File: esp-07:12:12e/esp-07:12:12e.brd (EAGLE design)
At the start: 40.3 x 38.1 mm, 5 parts, among them J1 ESP-STACK-HEADER

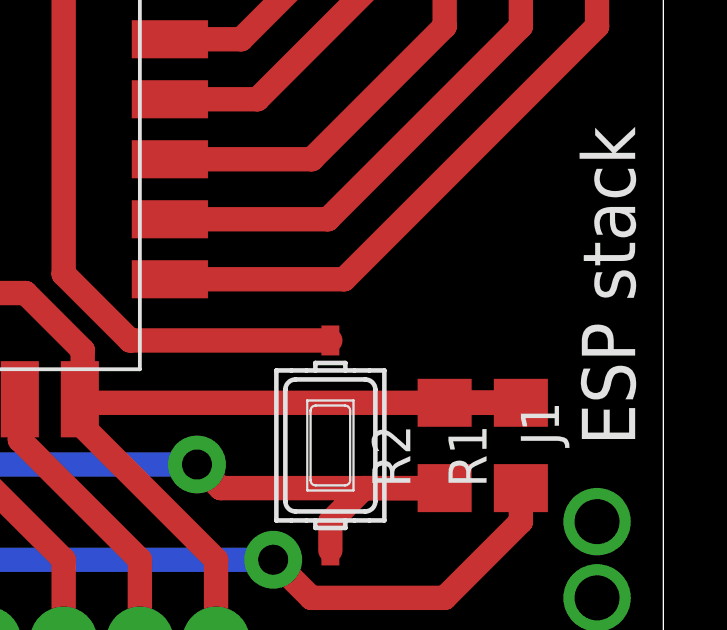
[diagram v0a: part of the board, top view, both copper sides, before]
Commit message: Added capacitor for power stability
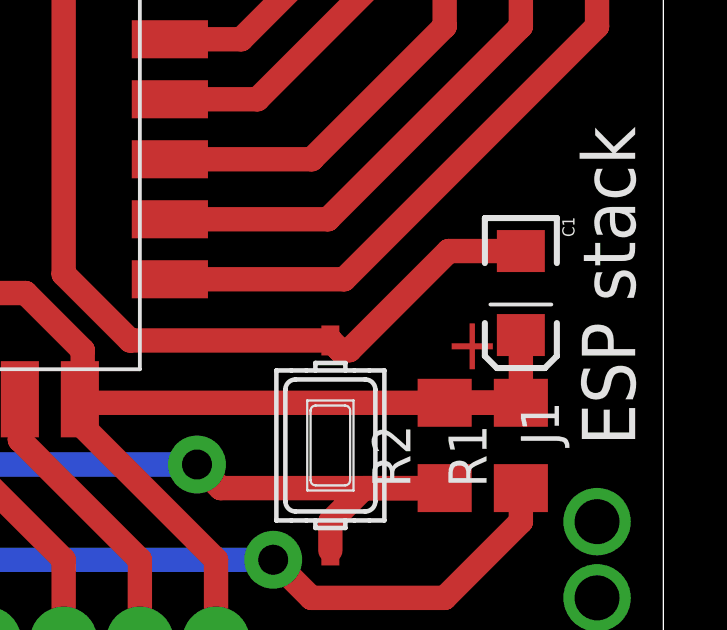
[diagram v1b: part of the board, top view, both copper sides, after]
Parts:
- added C1: 10uF, SparkFun-Capacitors:EIA3216
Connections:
- net +3V3: now also C1.A
- net GND: now also C1.C
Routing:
- net GND: track 56.0 -> 63.9 mm
- net +3V3: track 59.7 -> 61.9 mm
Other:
- board text added: "+"

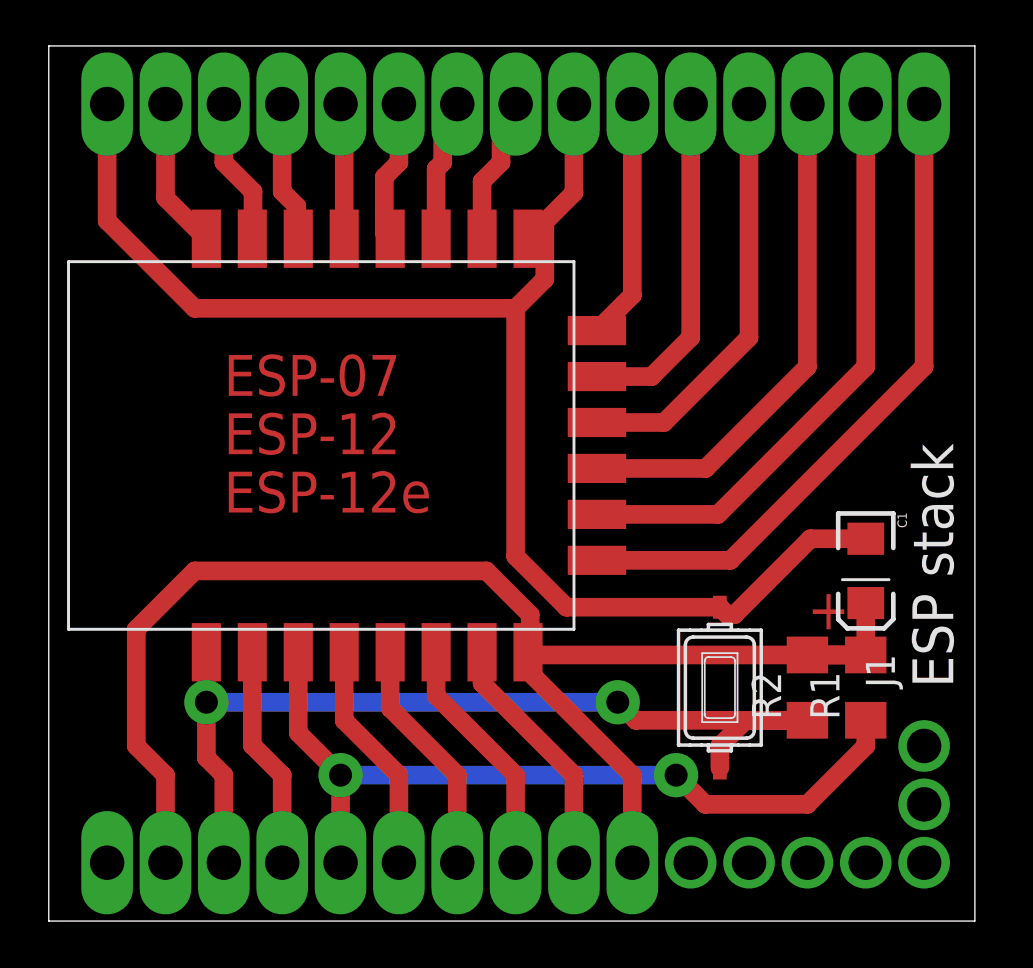
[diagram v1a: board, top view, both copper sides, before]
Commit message: Fix paths under ESP board - shouldn't overlap with module pads
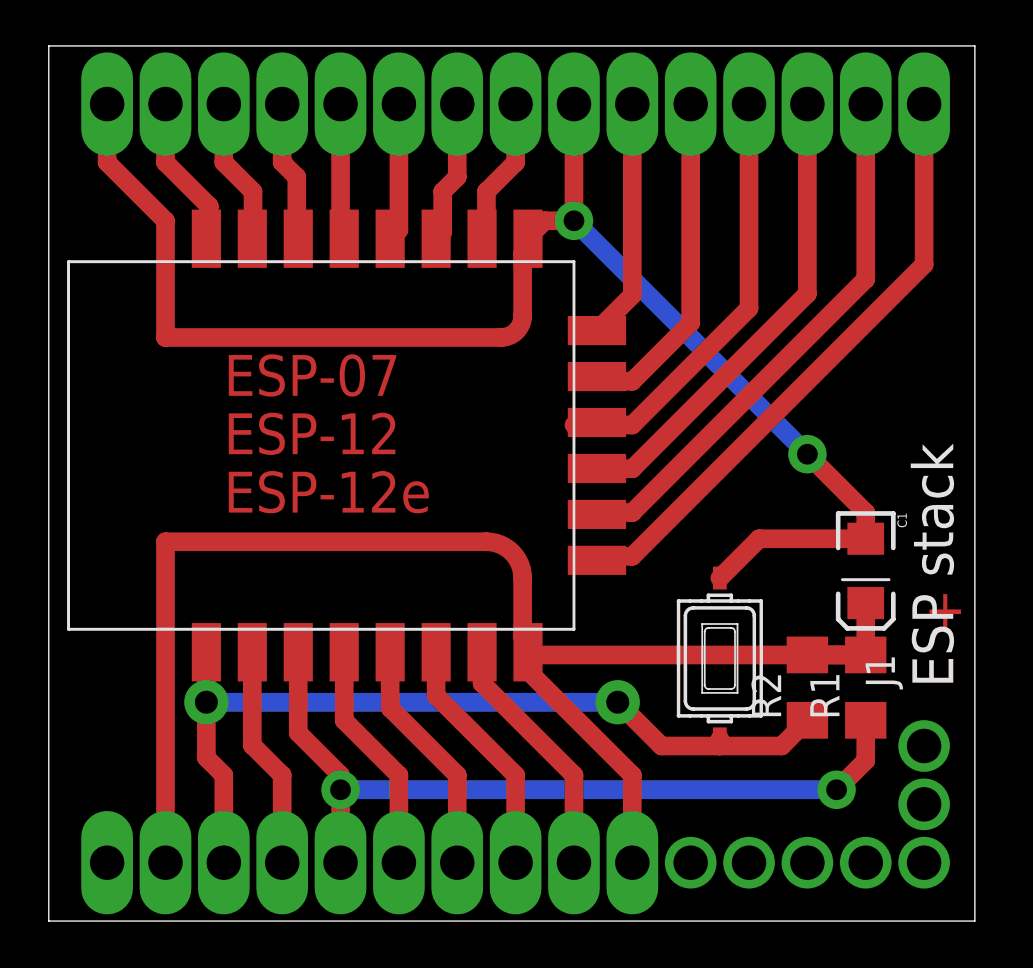
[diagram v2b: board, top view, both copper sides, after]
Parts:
- moved RESET 1.27 mm to (29.2, 11.4)
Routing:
- net RESET: track 41.2 -> 37.2 mm
- net CS0: track 29.2 -> 26.6 mm
- net MISO: track 25.8 -> 23.6 mm
- net +3V3: track 61.9 -> 64.1 mm
- net GPIO9: track 22.4 -> 20.6 mm
- net GND: track 63.9 -> 64.2 mm, vias 0 -> 2

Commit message: New board size - 1.4 inches; reduced number of signal pins to only two; mounting holes
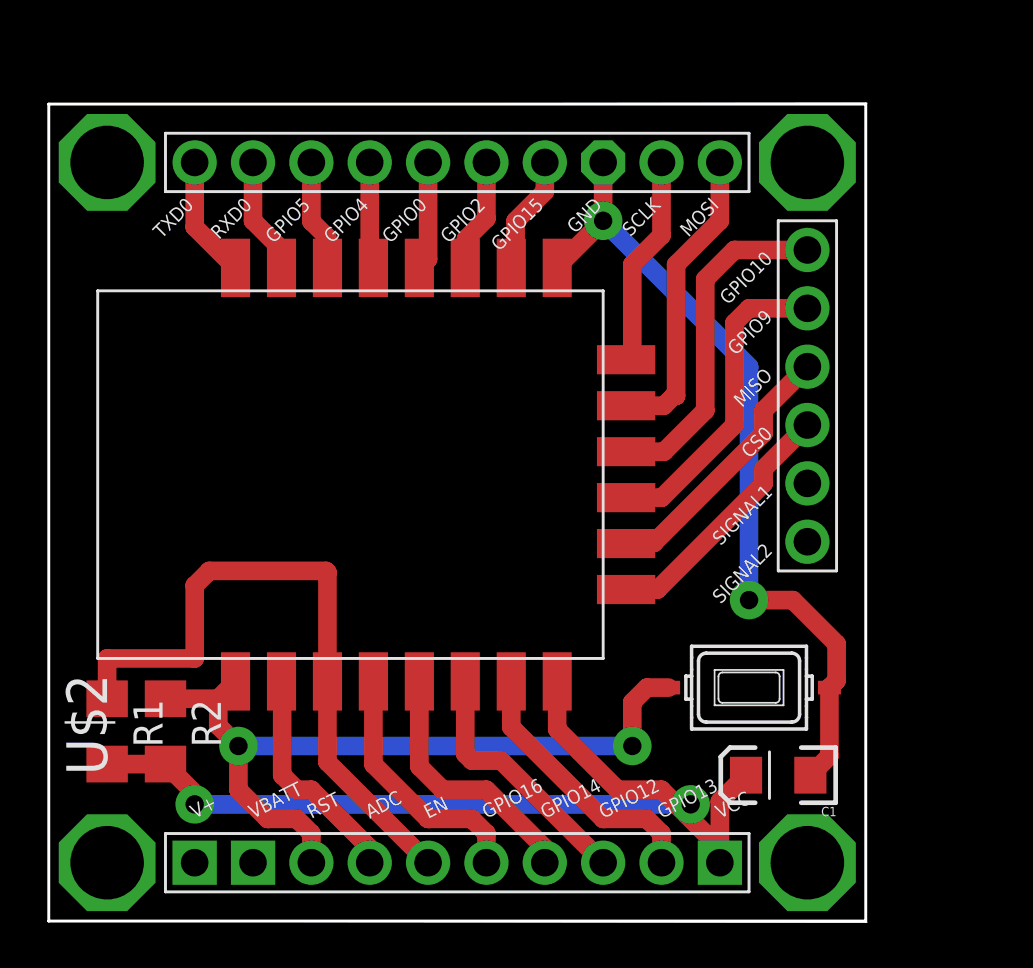
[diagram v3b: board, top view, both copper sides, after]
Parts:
- removed J1: ESP-STACK-HEADER, ESPstack:ESP-STACK-HEADER
- added U$2: ESP-BOARD, ESPstack:ESP-BOARD
- moved R1 33.1 mm to (2.54, 8.26), turned to 270 degrees
- moved R2 28.0 mm to (5.08, 8.26), turned to 270 degrees
- moved C1 9.67 mm to (31.8, 6.35), turned to 180 degrees
- moved RESET 1.80 mm to (30.5, 10.2), turned to 180 degrees
- moved U$1 1.80 mm to (24.1, 11.4)
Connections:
- new net VBATT: U$2.VBATT
- net +3V3: now also U$2.VCC; no longer J1.3V3@1, J1.3V3@2
- net ADC: now also U$2.ADC; no longer J1.ADC
- net CS0: now also U$2.CS0; no longer J1.CS0
- net EN: now also U$2.EN; no longer J1.EN
- net GND: now also U$2.GND@1, U$2.GND@2, U$2.GND@3, U$2.GND@4, U$2.GND@5; no longer J1.GND@1, J1.GND@2
- net GPIO0: now also U$2.GPIO0; no longer J1.GPIO0
- net GPIO10: now also U$2.GPIO10; no longer J1.GPIO10
- net GPIO12: now also U$2.GPIO12; no longer J1.GPIO12
- net GPIO13: now also U$2.GPIO13; no longer J1.GPIO13
- net GPIO14: now also U$2.GPIO14; no longer J1.GPIO14
- net GPIO15: now also U$2.GPIO15; no longer J1.GPIO15
- net GPIO16: now also U$2.GPIO16; no longer J1.GPIO16
- net GPIO2: now also U$2.GPIO2; no longer J1.GPIO2
- net GPIO4: now also U$2.GPIO4; no longer J1.GPIO4
- net GPIO5: now also U$2.GPIO5; no longer J1.GPIO5
- net GPIO9: now also U$2.GPIO9; no longer J1.GPIO9
- net MISO: now also U$2.MISO; no longer J1.MISO
- net MOSI: now also U$2.MOSI; no longer J1.MOSI
- net RESET: now also U$2.RST; no longer J1.RESET
- net RXD0: now also U$2.RXD0; no longer J1.RXD0
- net SCLK: now also U$2.SCLK; no longer J1.SCLK
- net TXD0: now also U$2.TXD0; no longer J1.TXD0
- net V+: now also U$2.V+; no longer J1.VBAT
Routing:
- net GND: track 64.2 -> 35.3 mm
- net +3V3: track 64.1 -> 43.1 mm, vias 0 -> 2
- net CS0: track 26.6 -> 11.2 mm
- net MISO: track 23.6 -> 11.7 mm
- net GPIO9: track 20.6 -> 13.9 mm
- net EN: track 35.1 -> 29.3 mm, vias 2 -> 0
- net GPIO10: track 18.8 -> 14.9 mm
- net RESET: track 37.2 -> 33.8 mm
- net MOSI: track 14.7 -> 13.3 mm
- net TXD0: track 6.70 -> 5.33 mm
- net GPIO2: track 6.24 -> 4.97 mm
- net GPIO4: track 5.93 -> 4.66 mm
- net GPIO15: track 6.46 -> 5.19 mm
- net GPIO0: track 6.02 -> 4.75 mm
- net GPIO5: track 6.15 -> 4.88 mm
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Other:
- board size 40.3 x 38.1 mm -> 35.6 x 35.7 mm
- board text removed: "+"
- board text removed: "ESP-07"
- board text removed: "ESP-12"
- board text removed: "ESP-12e"

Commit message: Small clearance improvements, bigger header pads and mounting holes
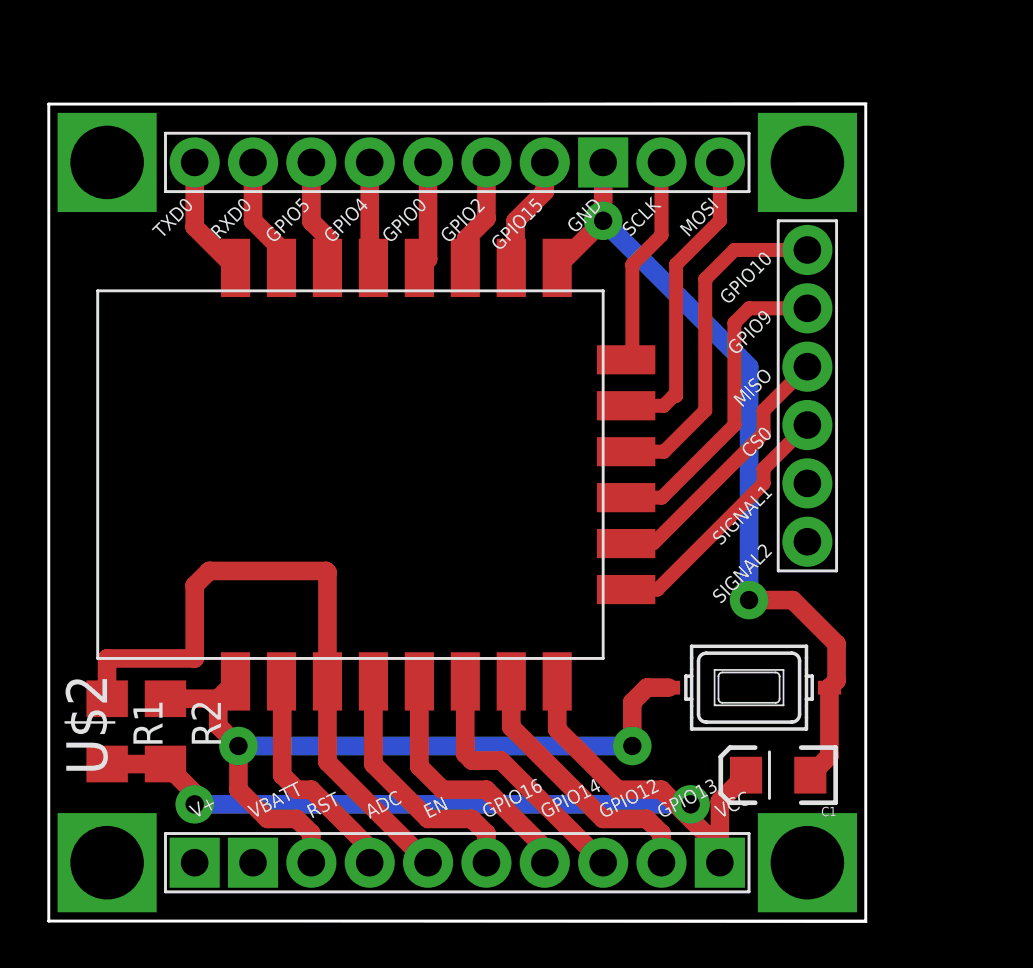
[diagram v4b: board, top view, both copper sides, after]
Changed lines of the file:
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@@
 <contactref element="U$1" pad="SCLK"/>
 <contactref element="U$2" pad="SCLK"/>
-<wire x1="26.67" y1="33.02" x2="26.67" y2="29.845" width="0.8128" layer="1"/>
-<wire x1="26.67" y1="29.845" x2="25.4" y2="28.575" width="0.8128" layer="1"/>
-<wire x1="25.4" y1="28.575" x2="25.4" y2="24.7" width="0.8128" layer="1"/>
+<wire x1="26.67" y1="33.02" x2="26.67" y2="29.845" width="0.6096" layer="1"/>
+<wire x1="26.67" y1="29.845" x2="25.4" y2="28.575" width="0.6096" layer="1"/>
+<wire x1="25.4" y1="28.575" x2="25.4" y2="24.7" width="0.6096" layer="1"/>
 <wire x1="25.4" y1="24.7" x2="25.13" y2="24.43" width="0.8128" layer="1"/>
 </signal>
@@
 <contactref element="U$1" pad="MOSI"/>
 <contactref element="U$2" pad="MOSI"/>
-<wire x1="29.21" y1="33.02" x2="29.21" y2="30.48" width="0.8128" layer="1"/>
-<wire x1="29.21" y1="30.48" x2="27.305" y2="28.575" width="0.8128" layer="1"/>
-<wire x1="27.305" y1="28.575" x2="27.305" y2="22.86" width="0.8128" layer="1"/>
-<wire x1="27.305" y1="22.86" x2="27.2034" y2="22.86" width="0.8128" layer="1"/>
-<wire x1="27.2034" y1="22.86" x2="26.7716" y2="22.4282" width="0.8128" layer="1"/>
-<wire x1="26.7716" y1="22.4282" x2="25.1318" y2="22.4282" width="0.8128" layer="1"/>
+<wire x1="29.21" y1="33.02" x2="29.21" y2="30.48" width="0.6096" layer="1"/>
+<wire x1="29.21" y1="30.48" x2="27.305" y2="28.575" width="0.6096" layer="1"/>
+<wire x1="27.305" y1="28.575" x2="27.305" y2="22.86" width="0.6096" layer="1"/>
+<wire x1="27.305" y1="22.86" x2="27.2034" y2="22.86" width="0.6096" layer="1"/>
+<wire x1="27.2034" y1="22.86" x2="26.7716" y2="22.4282" width="0.6096" layer="1"/>
+<wire x1="26.7716" y1="22.4282" x2="25.1318" y2="22.4282" width="0.6096" layer="1"/>
 <wire x1="25.1318" y1="22.4282" x2="25.13" y2="22.43" width="0.8128" layer="1"/>
 </signal>
@@
 <contactref element="U$1" pad="GPIO10"/>
 <contactref element="U$2" pad="GPIO10"/>
-<wire x1="25.13" y1="20.43" x2="26.78" y2="20.43" width="0.8128" layer="1"/>
-<wire x1="26.78" y1="20.43" x2="28.575" y2="22.225" width="0.8128" layer="1"/>
-<wire x1="28.575" y1="22.225" x2="28.575" y2="27.94" width="0.8128" layer="1"/>
-<wire x1="28.575" y1="27.94" x2="29.845" y2="29.21" width="0.8128" layer="1"/>
-<wire x1="29.845" y1="29.21" x2="33.02" y2="29.21" width="0.8128" layer="1"/>
+<wire x1="25.13" y1="20.43" x2="26.78" y2="20.43" width="0.6096" layer="1"/>
+<wire x1="26.78" y1="20.43" x2="28.575" y2="22.225" width="0.6096" layer="1"/>
+<wire x1="28.575" y1="22.225" x2="28.575" y2="27.94" width="0.6096" layer="1"/>
+<wire x1="28.575" y1="27.94" x2="29.845" y2="29.21" width="0.6096" layer="1"/>
+<wire x1="29.845" y1="29.21" x2="33.02" y2="29.21" width="0.6096" layer="1"/>
 </signal>
 <signal name="GPIO9">
 <contactref element="U$1" pad="GPIO9"/>
 <contactref element="U$2" pad="GPIO9"/>
-<wire x1="25.13" y1="18.43" x2="26.685" y2="18.43" width="0.8128" layer="1"/>
-<wire x1="26.685" y1="18.43" x2="29.845" y2="21.59" width="0.8128" layer="1"/>
-<wire x1="29.845" y1="21.59" x2="29.845" y2="26.035" width="0.8128" layer="1"/>
-<wire x1="29.845" y1="26.035" x2="30.48" y2="26.67" width="0.8128" layer="1"/>
-<wire x1="30.48" y1="26.67" x2="33.02" y2="26.67" width="0.8128" layer="1"/>
+<wire x1="25.13" y1="18.43" x2="26.685" y2="18.43" width="0.6096" layer="1"/>
+<wire x1="26.685" y1="18.43" x2="29.845" y2="21.59" width="0.6096" layer="1"/>
+<wire x1="29.845" y1="21.59" x2="29.845" y2="26.035" width="0.6096" layer="1"/>
+<wire x1="29.845" y1="26.035" x2="30.48" y2="26.67" width="0.6096" layer="1"/>
+<wire x1="30.48" y1="26.67" x2="33.02" y2="26.67" width="0.6096" layer="1"/>
 </signal>
 <signal name="MISO">
 <contactref element="U$1" pad="MISO"/>
 <contactref element="U$2" pad="MISO"/>
-<wire x1="33.02" y1="24.13" x2="31.115" y2="22.225" width="0.8128" layer="1"/>
-<wire x1="31.115" y1="22.225" x2="31.115" y2="21.2344" width="0.8128" layer="1"/>
-<wire x1="31.115" y1="21.2344" x2="26.3398" y2="16.4592" width="0.8128" layer="1"/>
-<wire x1="26.3398" y1="16.4592" x2="25.1592" y2="16.4592" width="0.8128" layer="1"/>
+<wire x1="33.02" y1="24.13" x2="31.115" y2="22.225" width="0.6096" layer="1"/>
+<wire x1="31.115" y1="22.225" x2="31.115" y2="21.2344" width="0.6096" layer="1"/>
+<wire x1="31.115" y1="21.2344" x2="26.3398" y2="16.4592" width="0.6096" layer="1"/>
+<wire x1="26.3398" y1="16.4592" x2="25.1592" y2="16.4592" width="0.6096" layer="1"/>
 <wire x1="25.1592" y1="16.4592" x2="25.13" y2="16.43" width="0.8128" layer="1"/>
 </signal>
@@
 <contactref element="U$1" pad="CSO"/>
 <contactref element="U$2" pad="CS0"/>
-<wire x1="25.13" y1="14.43" x2="26.495" y2="14.43" width="0.8128" layer="1"/>
-<wire x1="26.495" y1="14.43" x2="31.115" y2="19.05" width="0.8128" layer="1"/>
-<wire x1="31.115" y1="19.05" x2="31.115" y2="19.685" width="0.8128" layer="1"/>
-<wire x1="31.115" y1="19.685" x2="33.02" y2="21.59" width="0.8128" layer="1"/>
+<wire x1="25.13" y1="14.43" x2="26.495" y2="14.43" width="0.6096" layer="1"/>
+<wire x1="26.495" y1="14.43" x2="31.115" y2="19.05" width="0.6096" layer="1"/>
+<wire x1="31.115" y1="19.05" x2="31.115" y2="19.685" width="0.6096" layer="1"/>
+<wire x1="31.115" y1="19.685" x2="33.02" y2="21.59" width="0.6096" layer="1"/>
 </signal>
 <signal name="GPIO13">
